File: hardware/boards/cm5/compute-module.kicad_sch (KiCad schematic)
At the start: 6 parts, among them J101 10164227-1001A1RLF, J102 10164227-1001A1RLF, J103 BM04B-SRSS-TB

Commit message: feat(cm5): add the status light and short M.2 standoffs, space the rear ports
The side board grows to the main board's 102 mm depth, so the status light sits at the enclosure's front wall and the 2280 standoff clears the rear strip. RJ45, accessory and service USB-C now have even gaps with H4 between the USB-Cs and nRPIBOOT beside the service port. The status light is the main board's SK6812SIDE-A behind an SN74AHCT1G125 on GPIO10; H702 and H703 take 2230 and 2242 drives. The accessory ESD follows the main board's port cell, with TX1/TX2 polarity swapped at the receptacle as there.
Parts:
- added C103, C104: 100n, Capacitor_SMD:C_0402_1005Metric, symbol Device:C
- added D101: SK6812SIDE-A, Iasis:OPSCO_SK6812SIDE-A, symbol Iasis:SK6812SIDE-A
- added R102: 33, Resistor_SMD:R_0402_1005Metric, symbol Device:R
- added U101: SN74AHCT1G125DBVR, Package_TO_SOT_SMD:SOT-23-5, symbol 74xGxx:74AHCT1G125
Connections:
- net 5V: now also C103.1, C104.1, D101.2 (VDD), U101.5 (VCC)
- net GND: now also C103.2, C104.2, D101.4 (GND), U101.1, U101.3 (GND)
- net LED_DATA: now reaches J101.44 (GPIO10)
- net LED_DATA: now also U101.2
- new net: R102.1, U101.4
- new net: D101.1 (DIN), R102.2
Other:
- note added: "D101 sits at the front edge. GPIO10 (SPI0 MOSI) drives it through U101 at 5 V, as on the main board."
- note added: "Status light"

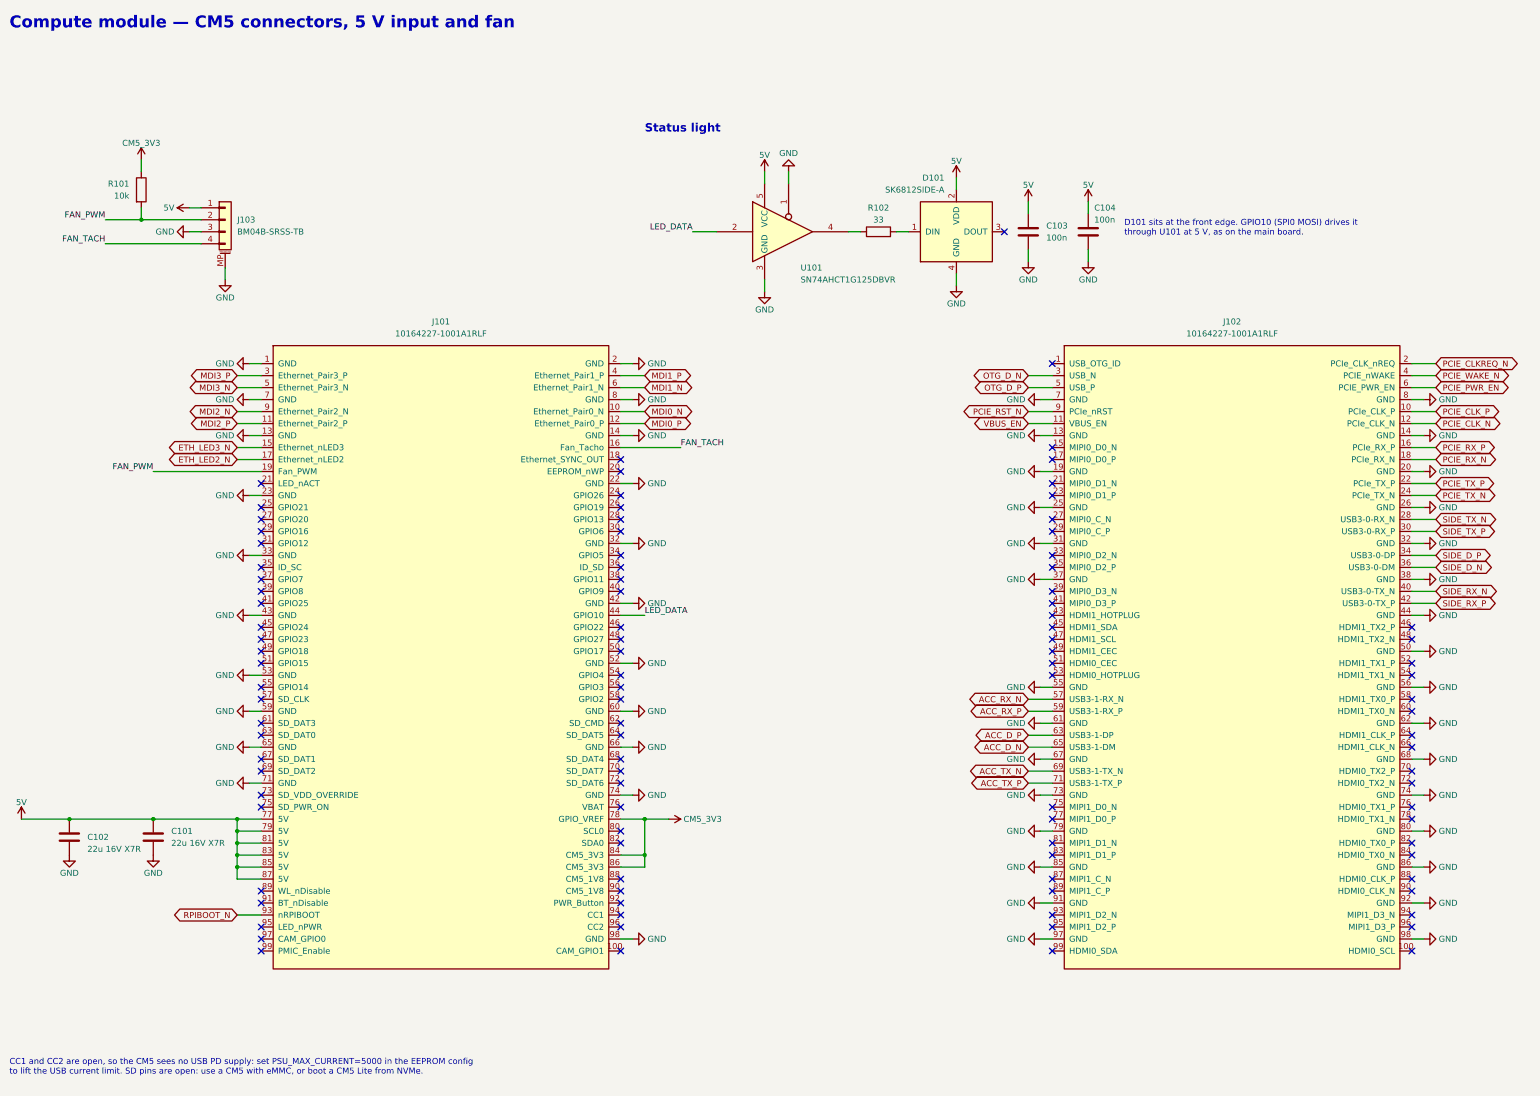
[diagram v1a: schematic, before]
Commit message: feat(cm5): route the side board
Every net routed and DRC clean with schematic parity. Pairs are length matched; slow lines run as
45-degree diagonals, with In3 carrying the long cross-board runs (RPIBOOT, CM5_3V3, the PCIe
sideband, VBUS_EN) under the outer layers' high-speed walls.

The board is 102 mm deep like the main board, with five mounting holes at the corners and beside
the rear ports. The service port joins its D pins over and under the receptacle's pad row, and
U501's CC channels follow the connector's order so both CC lines run straight to R501 and R502.
The jack LED resistors sit west of the jack, R101 beside the fan header and R406 beside Q401.
The MDI pairs have no ESD array, as on the CM5 IO board. SW501's twin pin-1 pads are marked as
jumpered.
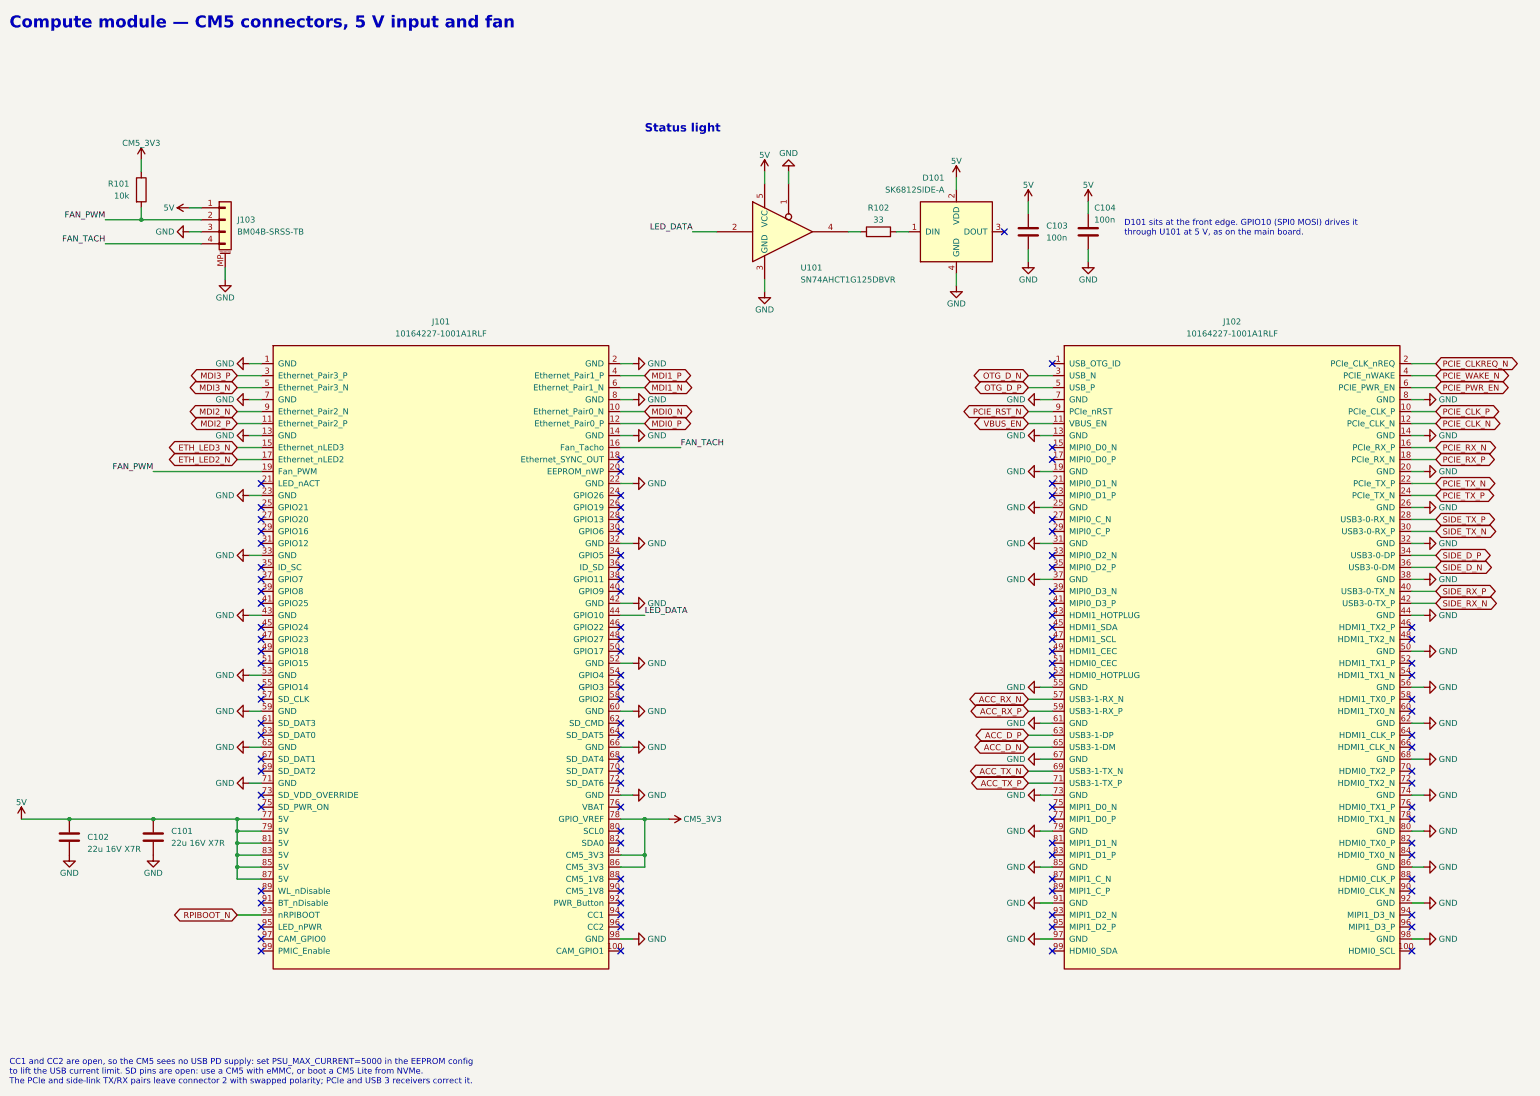
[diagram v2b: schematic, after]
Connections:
- net PCIE_RX_N: now also J102.16 (PCIe_RX_P); no longer J102.18 (PCIe_RX_N)
- net PCIE_RX_P: now also J102.18 (PCIe_RX_N); no longer J102.16 (PCIe_RX_P)
- net PCIE_TX_N: now also J102.22 (PCIe_TX_P); no longer J102.24 (PCIe_TX_N)
- net PCIE_TX_P: now also J102.24 (PCIe_TX_N); no longer J102.22 (PCIe_TX_P)
- net SIDE_RX_N: now also J102.42 (USB3-0-TX_P); no longer J102.40 (USB3-0-TX_N)
- net SIDE_RX_P: now also J102.40 (USB3-0-TX_N); no longer J102.42 (USB3-0-TX_P)
- net SIDE_TX_N: now also J102.30 (USB3-0-RX_P); no longer J102.28 (USB3-0-RX_N)
- net SIDE_TX_P: now also J102.28 (USB3-0-RX_N); no longer J102.30 (USB3-0-RX_P)
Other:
- note added: "CC1 and CC2 are open, so the CM5 sees no USB PD supply: set PSU_MAX_CURRENT=5000 in the EEPROM config to lift the USB current limit. SD pins are open: use a CM5 with eMMC, or boot a CM5 Lite from NVMe. The PCIe and side-link TX/RX pairs leave connector 2 with swapped polarity; PCIe and USB 3 receivers correct it."
- note removed: "CC1 and CC2 are open, so the CM5 sees no USB PD supply: set PSU_MAX_CURRENT=5000 in the EEPROM config to lift the USB current limit. SD pins are open: use a CM5 with eMMC, or boot a CM5 Lite from NVMe."
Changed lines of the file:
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@@
 (global_label "VBUS_EN" (shape bidirectional) (at 241.3 106.68 180) (effects (font (size 1.27 1.27)) (justify right)) (property "Intersheetrefs" "${INTERSHEET_REFS}" (at 241.3 106.68 0) (hide yes) (effects (font (size 1.27 1.27)))))
 (global_label "PCIE_CLK_N" (shape bidirectional) (at 327.66 106.68 0) (effects (font (size 1.27 1.27)) (justify left)) (property "Intersheetrefs" "${INTERSHEET_REFS}" (at 327.66 106.68 0) (hide yes) (effects (font (size 1.27 1.27)))))
-(global_label "PCIE_RX_P" (shape bidirectional) (at 327.66 111.76 0) (effects (font (size 1.27 1.27)) (justify left)) (property "Intersheetrefs" "${INTERSHEET_REFS}" (at 327.66 111.76 0) (hide yes) (effects (font (size 1.27 1.27)))))
-(global_label "PCIE_RX_N" (shape bidirectional) (at 327.66 114.3 0) (effects (font (size 1.27 1.27)) (justify left)) (property "Intersheetrefs" "${INTERSHEET_REFS}" (at 327.66 114.3 0) (hide yes) (effects (font (size 1.27 1.27)))))
-(global_label "PCIE_TX_P" (shape bidirectional) (at 327.66 119.38 0) (effects (font (size 1.27 1.27)) (justify left)) (property "Intersheetrefs" "${INTERSHEET_REFS}" (at 327.66 119.38 0) (hide yes) (effects (font (size 1.27 1.27)))))
-(global_label "PCIE_TX_N" (shape bidirectional) (at 327.66 121.92 0) (effects (font (size 1.27 1.27)) (justify left)) (property "Intersheetrefs" "${INTERSHEET_REFS}" (at 327.66 121.92 0) (hide yes) (effects (font (size 1.27 1.27)))))
-(global_label "SIDE_TX_N" (shape bidirectional) (at 327.66 127 0) (effects (font (size 1.27 1.27)) (justify left)) (property "Intersheetrefs" "${INTERSHEET_REFS}" (at 327.66 127 0) (hide yes) (effects (font (size 1.27 1.27)))))
-(global_label "SIDE_TX_P" (shape bidirectional) (at 327.66 129.54 0) (effects (font (size 1.27 1.27)) (justify left)) (property "Intersheetrefs" "${INTERSHEET_REFS}" (at 327.66 129.54 0) (hide yes) (effects (font (size 1.27 1.27)))))
+(global_label "PCIE_RX_N" (shape bidirectional) (at 327.66 111.76 0) (effects (font (size 1.27 1.27)) (justify left)) (property "Intersheetrefs" "${INTERSHEET_REFS}" (at 327.66 111.76 0) (hide yes) (effects (font (size 1.27 1.27)))))
+(global_label "PCIE_RX_P" (shape bidirectional) (at 327.66 114.3 0) (effects (font (size 1.27 1.27)) (justify left)) (property "Intersheetrefs" "${INTERSHEET_REFS}" (at 327.66 114.3 0) (hide yes) (effects (font (size 1.27 1.27)))))
+(global_label "PCIE_TX_N" (shape bidirectional) (at 327.66 119.38 0) (effects (font (size 1.27 1.27)) (justify left)) (property "Intersheetrefs" "${INTERSHEET_REFS}" (at 327.66 119.38 0) (hide yes) (effects (font (size 1.27 1.27)))))
+(global_label "PCIE_TX_P" (shape bidirectional) (at 327.66 121.92 0) (effects (font (size 1.27 1.27)) (justify left)) (property "Intersheetrefs" "${INTERSHEET_REFS}" (at 327.66 121.92 0) (hide yes) (effects (font (size 1.27 1.27)))))
+(global_label "SIDE_TX_P" (shape bidirectional) (at 327.66 127 0) (effects (font (size 1.27 1.27)) (justify left)) (property "Intersheetrefs" "${INTERSHEET_REFS}" (at 327.66 127 0) (hide yes) (effects (font (size 1.27 1.27)))))
+(global_label "SIDE_TX_N" (shape bidirectional) (at 327.66 129.54 0) (effects (font (size 1.27 1.27)) (justify left)) (property "Intersheetrefs" "${INTERSHEET_REFS}" (at 327.66 129.54 0) (hide yes) (effects (font (size 1.27 1.27)))))
 (global_label "SIDE_D_P" (shape bidirectional) (at 327.66 134.62 0) (effects (font (size 1.27 1.27)) (justify left)) (property "Intersheetrefs" "${INTERSHEET_REFS}" (at 327.66 134.62 0) (hide yes) (effects (font (size 1.27 1.27)))))
 (global_label "SIDE_D_N" (shape bidirectional) (at 327.66 137.16 0) (effects (font (size 1.27 1.27)) (justify left)) (property "Intersheetrefs" "${INTERSHEET_REFS}" (at 327.66 137.16 0) (hide yes) (effects (font (size 1.27 1.27)))))
-(global_label "SIDE_RX_N" (shape bidirectional) (at 327.66 142.24 0) (effects (font (size 1.27 1.27)) (justify left)) (property "Intersheetrefs" "${INTERSHEET_REFS}" (at 327.66 142.24 0) (hide yes) (effects (font (size 1.27 1.27)))))
-(global_label "SIDE_RX_P" (shape bidirectional) (at 327.66 144.78 0) (effects (font (size 1.27 1.27)) (justify left)) (property "Intersheetrefs" "${INTERSHEET_REFS}" (at 327.66 144.78 0) (hide yes) (effects (font (size 1.27 1.27)))))
+(global_label "SIDE_RX_P" (shape bidirectional) (at 327.66 142.24 0) (effects (font (size 1.27 1.27)) (justify left)) (property "Intersheetrefs" "${INTERSHEET_REFS}" (at 327.66 142.24 0) (hide yes) (effects (font (size 1.27 1.27)))))
+(global_label "SIDE_RX_N" (shape bidirectional) (at 327.66 144.78 0) (effects (font (size 1.27 1.27)) (justify left)) (property "Intersheetrefs" "${INTERSHEET_REFS}" (at 327.66 144.78 0) (hide yes) (effects (font (size 1.27 1.27)))))
 (global_label "ACC_RX_N" (shape bidirectional) (at 241.3 165.1 180) (effects (font (size 1.27 1.27)) (justify right)) (property "Intersheetrefs" "${INTERSHEET_REFS}" (at 241.3 165.1 0) (hide yes) (effects (font (size 1.27 1.27)))))
 (global_label "ACC_RX_P" (shape bidirectional) (at 241.3 167.64 180) (effects (font (size 1.27 1.27)) (justify right)) (property "Intersheetrefs" "${INTERSHEET_REFS}" (at 241.3 167.64 0) (hide yes) (effects (font (size 1.27 1.27)))))
@@
 (no_connect (at 322.58 218.44))
 (text "Compute module — CM5 connectors, 5 V input and fan" (exclude_from_sim no) (at 25.4 20.32 0) (effects (font (size 2.54 2.54) (bold yes)) (justify left top)))
-(text "CC1 and CC2 are open, so the CM5 sees no USB PD supply: set PSU_MAX_CURRENT=5000 in the EEPROM config\nto lift the USB current limit. SD pins are open: use a CM5 with eMMC, or boot a CM5 Lite from NVMe." (exclude_from_sim no) (at 25.4 241.3 0) (effects (font (size 1.27 1.27)) (justify left top)))
+(text "CC1 and CC2 are open, so the CM5 sees no USB PD supply: set PSU_MAX_CURRENT=5000 in the EEPROM config\nto lift the USB current limit. SD pins are open: use a CM5 with eMMC, or boot a CM5 Lite from NVMe.\nThe PCIe and side-link TX/RX pairs leave connector 2 with swapped polarity; PCIe and USB 3 receivers correct it." (exclude_from_sim no) (at 25.4 241.3 0) (effects (font (size 1.27 1.27)) (justify left top)))
 (text "Status light" (exclude_from_sim no) (at 160.02 43.18 0) (effects (font (size 1.778 1.778) (bold yes)) (justify left top)))
 (text "D101 sits at the front edge. GPIO10 (SPI0 MOSI) drives it\nthrough U101 at 5 V, as on the main board." (exclude_from_sim no) (at 261.62 63.5 0) (effects (font (size 1.27 1.27)) (justify left top)))
